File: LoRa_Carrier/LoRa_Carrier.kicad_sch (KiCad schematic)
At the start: 1 part, among them U1 RA-08H(915)

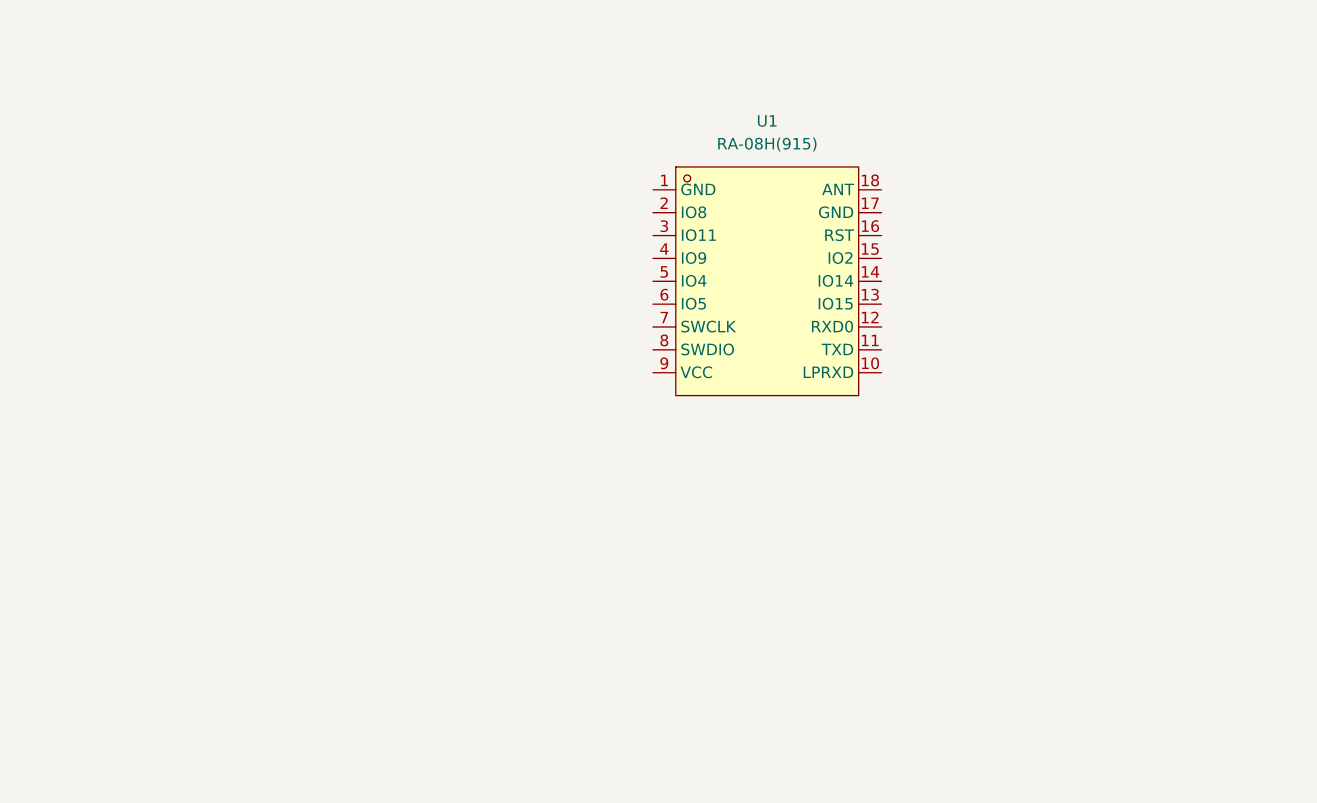
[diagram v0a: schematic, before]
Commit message: Finished Lora Carrier
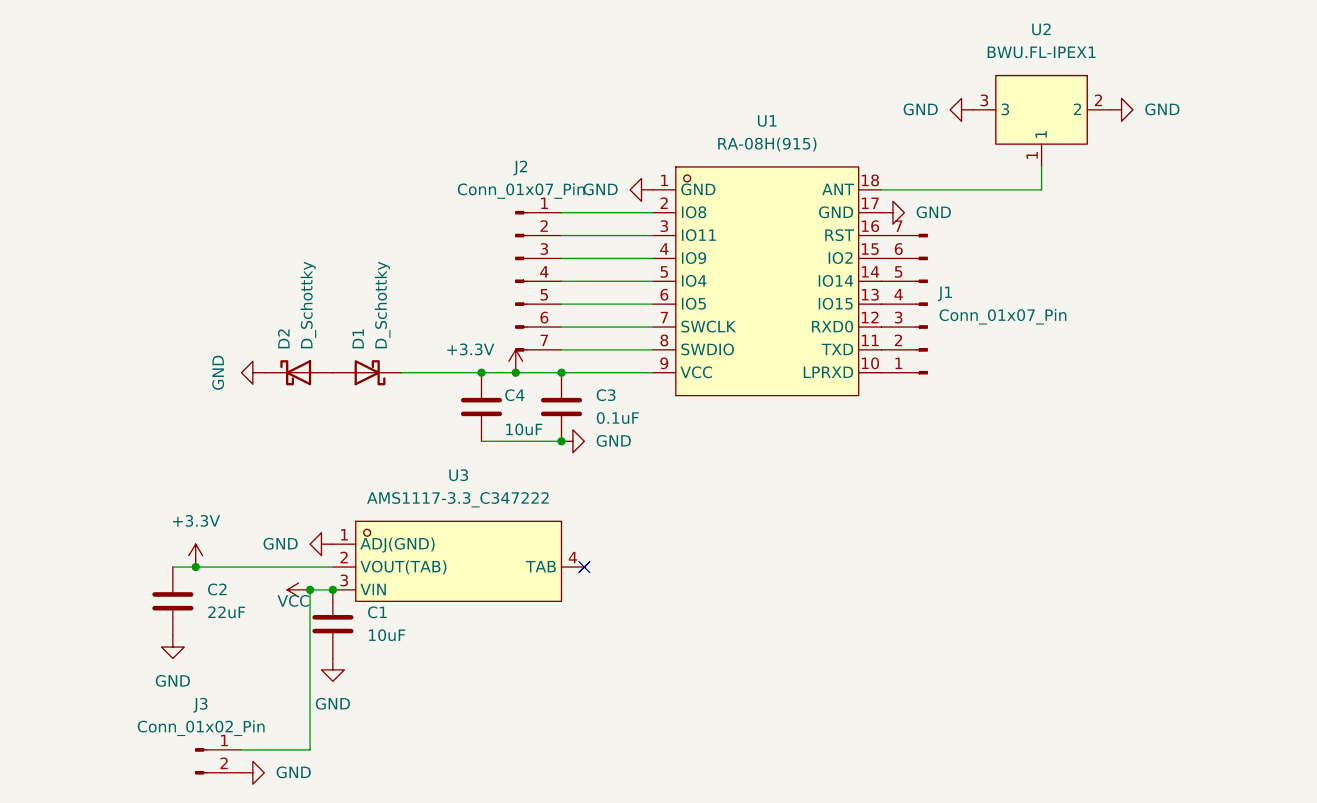
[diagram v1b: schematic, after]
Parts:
- added C1, C4: 10uF, Capacitor_SMD:C_0402_1005Metric, symbol Device:C
- added C2: 22uF, Capacitor_SMD:C_0805_2012Metric, symbol Device:C
- added C3: 0.1uF, Capacitor_SMD:C_1206_3216Metric, symbol Device:C
- added D1, D2: D_Schottky, Diode_SMD:D_SMA, symbol Device:D_Schottky
- added J1, J2: Conn_01x07_Pin, Connector_PinHeader_2.54mm:PinHeader_1x07_P2.54mm_Vertical, symbol Connector:Conn_01x07_Pin
- added J3: Conn_01x02_Pin, Connector_PinHeader_2.54mm:PinHeader_1x02_P2.54mm_Vertical, symbol Connector:Conn_01x02_Pin
- added U2: BWU.FL-IPEX1, PARTS:IPEX-SMD_BWIPX-1-001E, symbol PARTS:BWU.FL-IPEX1
- added U3: AMS1117-3.3_C347222, PARTS:SOT-223-4_L6.5-W3.5-P2.30-LS7.0-BR, symbol PARTS:AMS1117-3.3_C347222
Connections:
- net GND: now reaches U1.1 (GND)
- net GND: now also U1.17 (GND), C1.2, C2.2, C3.2, C4.2, D2.1 (K), J3.2 (Pin_2), U2.2, U2.3, U3.1 (ADJ(GND))
- net at U1.10 (LPRXD): now also J1.1 (Pin_1)
- net at U1.11 (TXD): now also J1.2 (Pin_2)
- net at U1.12 (RXD0): now also J1.3 (Pin_3)
- net at U1.13 (IO15): now also J1.4 (Pin_4)
- net at U1.14 (IO14): now also J1.5 (Pin_5)
- net at U1.15 (IO2): now also J1.6 (Pin_6)
- net at U1.16 (RST): now also J1.7 (Pin_7)
- net at U1.18 (ANT): now also U2.1
- net at U1.2 (IO8): now also J2.1 (Pin_1)
- net at U1.3 (IO11): now also J2.2 (Pin_2)
- net at U1.4 (IO9): now also J2.3 (Pin_3)
- net at U1.5 (IO4): now also J2.4 (Pin_4)
- net at U1.6 (IO5): now also J2.5 (Pin_5)
- net at U1.7 (SWCLK): now also J2.6 (Pin_6)
- net at U1.8 (SWDIO): now also J2.7 (Pin_7)
- net +3.3V: now reaches U1.9 (VCC)
- net +3.3V: now also C2.1, C3.1, C4.1, D1.1 (K), U3.2 (VOUT(TAB))
- new net: D1.2 (A), D2.2 (A)
- new net VCC: C1.1, J3.1 (Pin_1), U3.3 (VIN)
- no-connect marks 0 -> 1

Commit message: Reworked Lora Carrier.
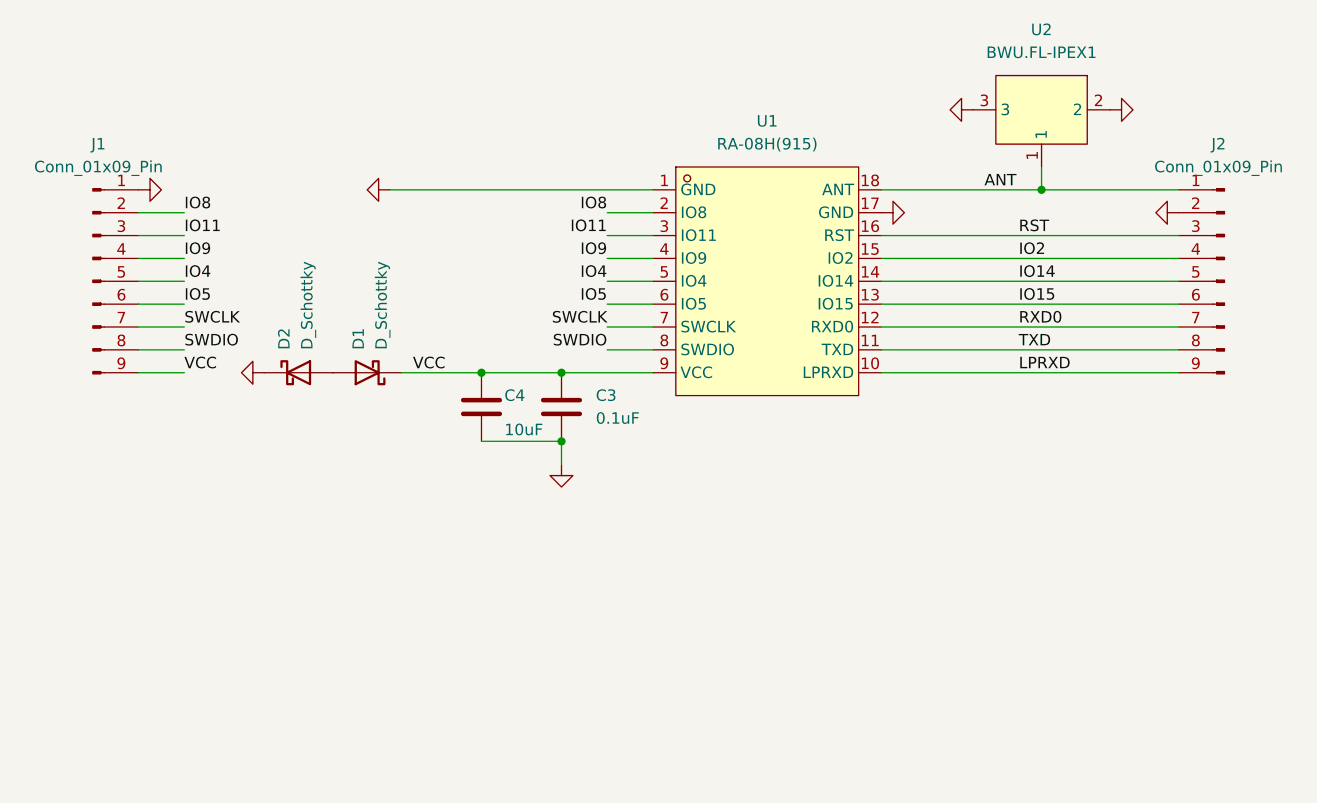
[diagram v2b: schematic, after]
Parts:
- removed C1: 10uF, Capacitor_SMD:C_0402_1005Metric, symbol Device:C
- removed C2: 22uF, Capacitor_SMD:C_0805_2012Metric, symbol Device:C
- removed J1, J2: Conn_01x07_Pin, Connector_PinHeader_2.54mm:PinHeader_1x07_P2.54mm_Vertical, symbol Connector:Conn_01x07_Pin
- removed J3: Conn_01x02_Pin, Connector_PinHeader_2.54mm:PinHeader_1x02_P2.54mm_Vertical, symbol Connector:Conn_01x02_Pin
- removed U3: AMS1117-3.3_C347222, PARTS:SOT-223-4_L6.5-W3.5-P2.30-LS7.0-BR, symbol PARTS:AMS1117-3.3_C347222
- added J1, J2: Conn_01x09_Pin, Connector_PinHeader_2.54mm:PinHeader_1x09_P2.54mm_Vertical, symbol Connector:Conn_01x09_Pin
- C3: footprint Capacitor_SMD:C_1206_3216Metric -> Capacitor_SMD:C_0402_1005Metric
- D1, D2: footprint Diode_SMD:D_SMA -> Diode_SMD:D_SOD-523
- U1: footprint PARTS:RA_08H-BREAKOUT -> PARTS:COMM-SMD_18P-L16.0-W16.0-P1.27-BL_RA-08H
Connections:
- net +3.3V is gone; now on net VCC: C3.1, C4.1, D1.1 (K), U1.9 (VCC)
- net GND: now also J1.1 (Pin_1), J2.2 (Pin_2)
- net VCC: now also J1.9 (Pin_9)
- net ANT: now reaches U1.18 (ANT), U2.1
- net ANT: now also J2.1 (Pin_1)
- net IO8: now reaches U1.2 (IO8)
- net IO8: now also J1.2 (Pin_2)
- net IO11: now reaches U1.3 (IO11)
- net IO11: now also J1.3 (Pin_3)
- net IO9: now reaches U1.4 (IO9)
- net IO9: now also J1.4 (Pin_4)
- net IO4: now reaches U1.5 (IO4)
- net IO4: now also J1.5 (Pin_5)
- net IO5: now reaches U1.6 (IO5)
- net IO5: now also J1.6 (Pin_6)
- net SWCLK: now reaches U1.7 (SWCLK)
- net SWCLK: now also J1.7 (Pin_7)
- net SWDIO: now reaches U1.8 (SWDIO)
- net SWDIO: now also J1.8 (Pin_8)
- net LPRXD: now reaches U1.10 (LPRXD)
- net LPRXD: now also J2.9 (Pin_9)
- net TXD: now reaches U1.11 (TXD)
- net TXD: now also J2.8 (Pin_8)
- net RXD0: now reaches U1.12 (RXD0)
- net RXD0: now also J2.7 (Pin_7)
- net IO15: now reaches U1.13 (IO15)
- net IO15: now also J2.6 (Pin_6)
- net IO14: now reaches U1.14 (IO14)
- net IO14: now also J2.5 (Pin_5)
- net IO2: now reaches U1.15 (IO2)
- net IO2: now also J2.4 (Pin_4)
- net RST: now reaches U1.16 (RST)
- net RST: now also J2.3 (Pin_3)
- no-connect marks 1 -> 0
